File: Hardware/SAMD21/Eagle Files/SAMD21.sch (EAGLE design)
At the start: 27 parts, among them SW1 SPST_TACT-KMR2, U1 ATSAMD21G-A, U2 SPX3819-3.3, U3 MCP73831T-2ACI/OT, X1 JSTPH, X3 microUSB, Y1 32.768kHz

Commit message: Agrega JTAG a SAMD21
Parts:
- added J1: (no value), SparkFun-Connectors:M05X2SHD_LOCK
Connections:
- new net N$3: J1.1, U1.PA30(SWCLK/SER1:2+)
- new net N$5: J1.5, U1.PA31(SWDIO/SER1:3+)
- new net N$6: J1.2
- net !RESET: now also J1.6
- net OUT: now also J1.4
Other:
- moved on the sheet: C8, R2, R3, SW1
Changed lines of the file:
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@@
 <part name="C12" library="microbuilder" deviceset="CAP_CERAMIC" device="0805-NOOUTLINE" value="10µF"/>
 <part name="R8" library="microbuilder" deviceset="RESISTOR" device="_0603_NOOUT" value="10K\"/>
+<part name="J1" library="SparkFun-Connectors" deviceset="M05X2" device="SHD_LOCK"/>
 </parts>
 <sheets>
@@
 <instance part="C4" gate="G$1" x="12.7" y="78.74" rot="MR0"/>
 <instance part="C7" gate="G$1" x="116.84" y="78.74" rot="MR0"/>
-<instance part="C8" gate="G$1" x="38.1" y="101.6" rot="MR0"/>
+<instance part="C8" gate="G$1" x="38.1" y="104.14" rot="MR0"/>
 <instance part="X3" gate="G$1" x="-124.46" y="111.76"/>
 <instance part="C9" gate="G$1" x="-68.58" y="104.14"/>
@@
 <instance part="X1" gate="G$1" x="-78.74" y="83.82" rot="R270"/>
 <instance part="R1" gate="G$1" x="-63.5" y="111.76" rot="R270"/>
-<instance part="SW1" gate="G$1" x="50.8" y="114.3" smashed="yes" rot="R270">
-<attribute name="NAME" x="48.26" y="120.65" size="1.778" layer="95"/>
+<instance part="SW1" gate="G$1" x="50.8" y="116.84" smashed="yes" rot="R270">
+<attribute name="NAME" x="48.26" y="123.19" size="1.778" layer="95"/>
 </instance>
-<instance part="R2" gate="G$1" x="55.88" y="104.14" rot="R90"/>
-<instance part="R3" gate="G$1" x="38.1" y="119.38" rot="R90"/>
+<instance part="R2" gate="G$1" x="55.88" y="106.68" rot="R90"/>
+<instance part="R3" gate="G$1" x="38.1" y="121.92" rot="R90"/>
 <instance part="U3" gate="G$1" x="-106.68" y="58.42"/>
 <instance part="CHG" gate="G$1" x="-129.54" y="63.5" rot="R270"/>
@@
 <instance part="C12" gate="G$1" x="-73.66" y="53.34"/>
 <instance part="R8" gate="G$1" x="-83.82" y="58.42"/>
+<instance part="J1" gate="G$1" x="154.94" y="53.34"/>
 </instances>
 <busses>
@@
 <pinref part="R2" gate="G$1" pin="1"/>
 <pinref part="C8" gate="G$1" pin="2"/>
-<wire x1="55.88" y1="99.06" x2="48.26" y2="99.06" width="0.1524" layer="91"/>
-<wire x1="48.26" y1="99.06" x2="38.1" y2="99.06" width="0.1524" layer="91"/>
-<wire x1="48.26" y1="99.06" x2="48.26" y2="96.52" width="0.1524" layer="91"/>
-<junction x="48.26" y="99.06"/>
-<label x="48.26" y="96.52" size="1.778" layer="95"/>
+<wire x1="55.88" y1="101.6" x2="48.26" y2="101.6" width="0.1524" layer="91"/>
+<wire x1="48.26" y1="101.6" x2="38.1" y2="101.6" width="0.1524" layer="91"/>
+<wire x1="48.26" y1="101.6" x2="48.26" y2="99.06" width="0.1524" layer="91"/>
+<junction x="48.26" y="101.6"/>
+<label x="48.26" y="99.06" size="1.778" layer="95"/>
 </segment>
 <segment>
@@
 <net name="!RESET" class="0">
 <segment>
-<wire x1="45.72" y1="111.76" x2="45.72" y2="114.3" width="0.1524" layer="91"/>
+<wire x1="45.72" y1="114.3" x2="45.72" y2="116.84" width="0.1524" layer="91"/>
 <pinref part="SW1" gate="G$1" pin="P"/>
 <pinref part="SW1" gate="G$1" pin="P1"/>
 <pinref part="C8" gate="G$1" pin="1"/>
-<wire x1="38.1" y1="106.68" x2="38.1" y2="111.76" width="0.1524" layer="91"/>
-<wire x1="38.1" y1="111.76" x2="45.72" y2="111.76" width="0.1524" layer="91"/>
-<junction x="45.72" y="111.76"/>
+<wire x1="38.1" y1="109.22" x2="38.1" y2="114.3" width="0.1524" layer="91"/>
+<wire x1="38.1" y1="114.3" x2="45.72" y2="114.3" width="0.1524" layer="91"/>
+<junction x="45.72" y="114.3"/>
 <pinref part="U1" gate="G$1" pin="!RESET!"/>
 <wire x1="33.02" y1="88.9" x2="27.94" y2="88.9" width="0.1524" layer="91"/>
-<wire x1="27.94" y1="88.9" x2="27.94" y2="111.76" width="0.1524" layer="91"/>
-<wire x1="27.94" y1="111.76" x2="38.1" y2="111.76" width="0.1524" layer="91"/>
-<junction x="38.1" y="111.76"/>
+<wire x1="27.94" y1="88.9" x2="27.94" y2="93.98" width="0.1524" layer="91"/>
+<wire x1="27.94" y1="93.98" x2="27.94" y2="114.3" width="0.1524" layer="91"/>
+<wire x1="27.94" y1="114.3" x2="38.1" y2="114.3" width="0.1524" layer="91"/>
+<junction x="38.1" y="114.3"/>
 <pinref part="R3" gate="G$1" pin="1"/>
-<wire x1="38.1" y1="114.3" x2="38.1" y2="111.76" width="0.1524" layer="91"/>
+<wire x1="38.1" y1="116.84" x2="38.1" y2="114.3" width="0.1524" layer="91"/>
+<wire x1="27.94" y1="93.98" x2="172.72" y2="93.98" width="0.1524" layer="91"/>
+<wire x1="172.72" y1="93.98" x2="172.72" y2="53.34" width="0.1524" layer="91"/>
+<junction x="27.94" y="93.98"/>
+<pinref part="J1" gate="G$1" pin="6"/>
+<wire x1="172.72" y1="53.34" x2="162.56" y2="53.34" width="0.1524" layer="91"/>
 </segment>
 </net>
@@
 <pinref part="SW1" gate="G$1" pin="S"/>
 <pinref part="SW1" gate="G$1" pin="S1"/>
-<wire x1="55.88" y1="114.3" x2="55.88" y2="111.76" width="0.1524" layer="91"/>
+<wire x1="55.88" y1="116.84" x2="55.88" y2="114.3" width="0.1524" layer="91"/>
 <pinref part="R2" gate="G$1" pin="2"/>
-<wire x1="55.88" y1="109.22" x2="55.88" y2="111.76" width="0.1524" layer="91"/>
-<junction x="55.88" y="111.76"/>
+<wire x1="55.88" y1="111.76" x2="55.88" y2="114.3" width="0.1524" layer="91"/>
+<junction x="55.88" y="114.3"/>
 </segment>
 </net>
@@
 <wire x1="116.84" y1="129.54" x2="116.84" y2="86.36" width="0.1524" layer="91"/>
 <pinref part="R3" gate="G$1" pin="2"/>
-<wire x1="38.1" y1="129.54" x2="38.1" y2="124.46" width="0.1524" layer="91"/>
+<wire x1="38.1" y1="129.54" x2="38.1" y2="127" width="0.1524" layer="91"/>
 <junction x="38.1" y="129.54"/>
-</segment>
-</net>
+<pinref part="J1" gate="G$1" pin="4"/>
+<wire x1="162.56" y1="55.88" x2="170.18" y2="55.88" width="0.1524" layer="91"/>
+<wire x1="170.18" y1="55.88" x2="170.18" y2="86.36" width="0.1524" layer="91"/>
+<wire x1="170.18" y1="86.36" x2="116.84" y2="86.36" width="0.1524" layer="91"/>
+</segment>
+</net>
+<net name="N$3" class="0">
+<segment>
+<pinref part="U1" gate="G$1" pin="PA30(SWCLK/SER1:2+)"/>
+<wire x1="101.6" y1="30.48" x2="119.38" y2="30.48" width="0.1524" layer="91"/>
+<wire x1="119.38" y1="30.48" x2="119.38" y2="58.42" width="0.1524" layer="91"/>
+<pinref part="J1" gate="G$1" pin="1"/>
+<wire x1="119.38" y1="58.42" x2="147.32" y2="58.42" width="0.1524" layer="91"/>
+</segment>
+</net>
+<net name="N$5" class="0">
+<segment>
+<pinref part="U1" gate="G$1" pin="PA31(SWDIO/SER1:3+)"/>
+<wire x1="101.6" y1="27.94" x2="121.92" y2="27.94" width="0.1524" layer="91"/>
+<wire x1="121.92" y1="27.94" x2="121.92" y2="53.34" width="0.1524" layer="91"/>
+<pinref part="J1" gate="G$1" pin="5"/>
+<wire x1="121.92" y1="53.34" x2="147.32" y2="53.34" width="0.1524" layer="91"/>
+</segment>
+</net>
+<net name="N$6" class="0">
+<segment>
+<pinref part="J1" gate="G$1" pin="2"/>
+<wire x1="162.56" y1="58.42" x2="167.64" y2="58.42" width="0.1524" layer="91"/>
+</segment>
+</net>

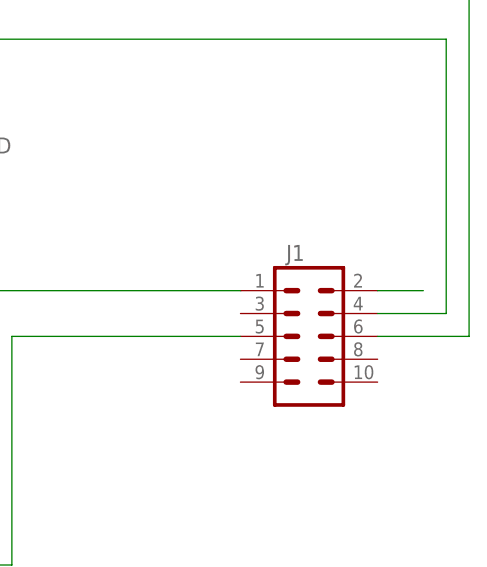
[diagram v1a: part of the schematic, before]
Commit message: Corrige error en tierra de JTAG para SAMD21
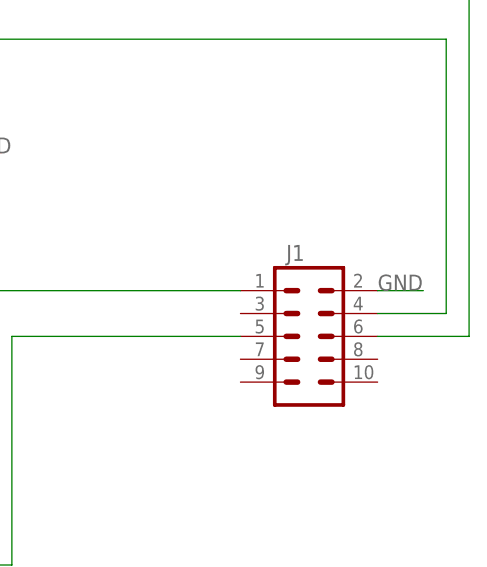
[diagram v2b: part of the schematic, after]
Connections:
- removed net N$6: J1.2
- net GND: now also J1.2
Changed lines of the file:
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@@
 <label x="-73.66" y="48.26" size="1.778" layer="95"/>
+</segment>
+<segment>
+<pinref part="J1" gate="G$1" pin="2"/>
+<wire x1="162.56" y1="58.42" x2="167.64" y2="58.42" width="0.1524" layer="91"/>
+<label x="162.56" y="58.42" size="1.778" layer="95"/>
 </segment>
 </net>
@@
 </segment>
 </net>
-<net name="N$6" class="0">
-<segment>
-<pinref part="J1" gate="G$1" pin="2"/>
-<wire x1="162.56" y1="58.42" x2="167.64" y2="58.42" width="0.1524" layer="91"/>
-</segment>
-</net>
